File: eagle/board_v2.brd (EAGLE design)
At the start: 104.4 x 80.6 mm, 34 parts, among them J1 RJ11-4X, Q1 BD140, Q10 BD140, Q11 BD140, Q12 BD140, Q13 BD140, Q14 BD140, Q15 BD140, Q2 BD140, Q3 BD140, Q4 BD140, Q5 BD140, Q6 BD140, Q7 BD140, Q8 BD140, Q9 BD140, X1 RJ45-8X, X2 RJ45-8X, X3 RJ45-8X, X4 RJ45-8X, X5 RJ45-8X

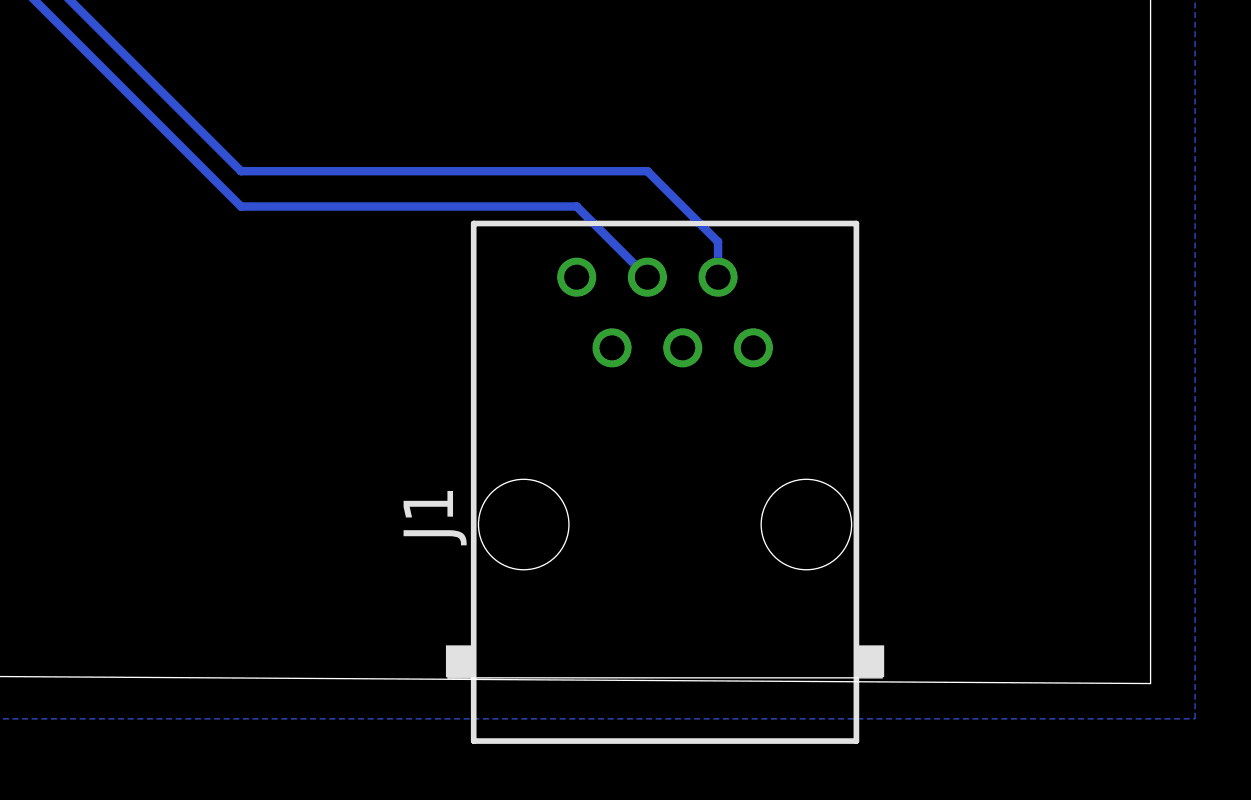
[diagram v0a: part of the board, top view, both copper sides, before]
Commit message: board chaining connectors
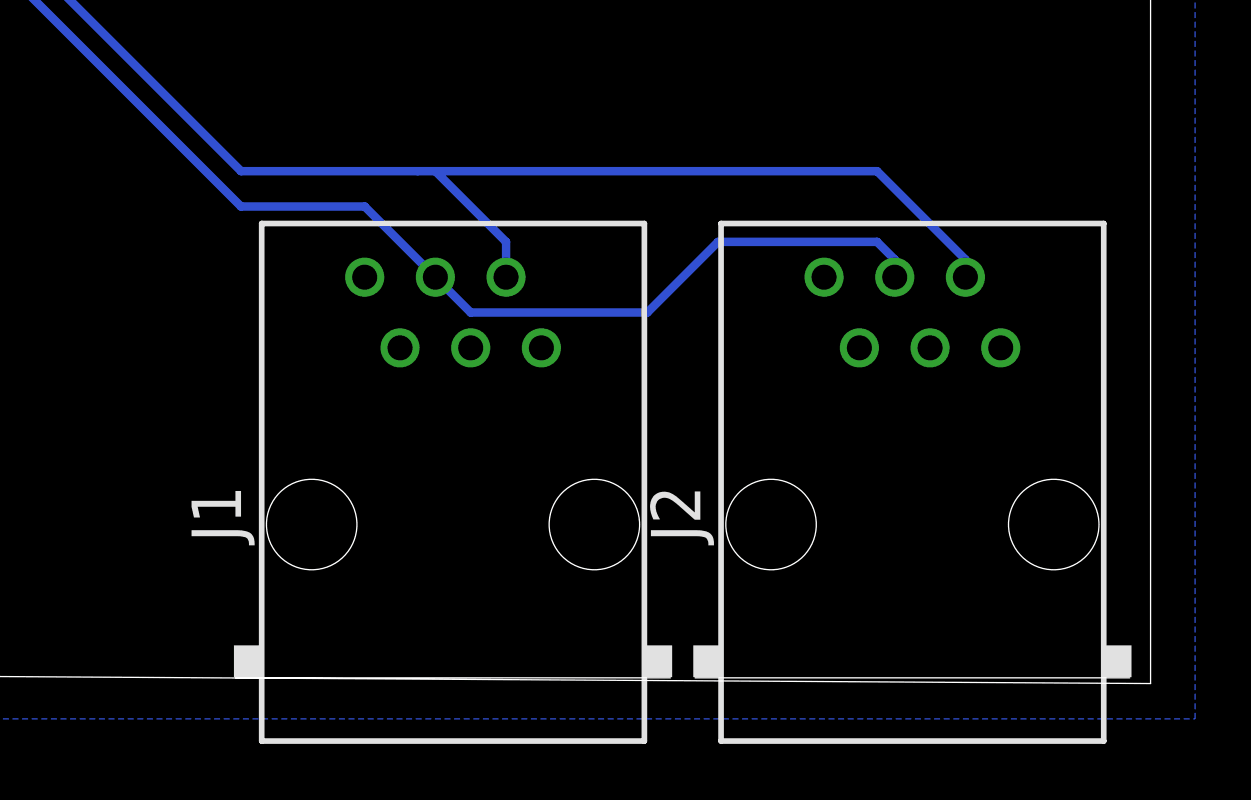
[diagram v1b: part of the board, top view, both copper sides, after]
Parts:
- added J2: RJ11-4X, con-tycoelectronics:RJ11-NO_SHIELD
- moved J1 7.62 mm to (79.4, 5.08)
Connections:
- net GND: now also J2.2, J2.4
- net N$37: now also J2.5
- net N$38: now also J2.3
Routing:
- net N$37: track 69.6 -> 83.0 mm
- net N$38: track 52.4 -> 63.8 mm
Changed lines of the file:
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@@
 <attribute name="OC_FARNELL" value="9471570" x="26.035" y="26.035" size="1.778" layer="27" rot="R90" display="off"/>
 </element>
-<element name="J1" library="con-tycoelectronics" package="RJ11-NO_SHIELD" value="RJ11-4X" x="86.995" y="5.08">
-<attribute name="OC_NEWARK" value="19R7022" x="86.995" y="5.08" size="2.54" layer="27" font="vector" display="off"/>
-<attribute name="MPN" value="6609214-3" x="86.995" y="5.08" size="2.54" layer="27" font="vector" display="off"/>
-<attribute name="MF" value="" x="86.995" y="5.08" size="2.54" layer="27" font="vector" display="off"/>
-<attribute name="OC_FARNELL" value="unknown" x="86.995" y="5.08" size="2.54" layer="27" font="vector" display="off"/>
+<element name="J1" library="con-tycoelectronics" package="RJ11-NO_SHIELD" value="RJ11-4X" x="79.375" y="5.08">
+<attribute name="OC_NEWARK" value="19R7022" x="79.375" y="5.08" size="2.54" layer="27" font="vector" display="off"/>
+<attribute name="MPN" value="6609214-3" x="79.375" y="5.08" size="2.54" layer="27" font="vector" display="off"/>
+<attribute name="MF" value="" x="79.375" y="5.08" size="2.54" layer="27" font="vector" display="off"/>
+<attribute name="OC_FARNELL" value="unknown" x="79.375" y="5.08" size="2.54" layer="27" font="vector" display="off"/>
+</element>
+<element name="J2" library="con-tycoelectronics" package="RJ11-NO_SHIELD" value="RJ11-4X" x="95.885" y="5.08">
+<attribute name="OC_NEWARK" value="19R7022" x="95.885" y="5.08" size="1.778" layer="27" display="off"/>
+<attribute name="MPN" value="6609214-3" x="95.885" y="5.08" size="1.778" layer="27" display="off"/>
+<attribute name="MF" value="" x="95.885" y="5.08" size="1.778" layer="27" display="off"/>
+<attribute name="OC_FARNELL" value="unknown" x="95.885" y="5.08" size="1.778" layer="27" display="off"/>
 </element>
 </elements>
@@
 <contactref element="J1" pad="4"/>
 <contactref element="J1" pad="2"/>
+<contactref element="J2" pad="4"/>
+<contactref element="J2" pad="2"/>
 </signal>
 <signal name="N$4">
@@
 <wire x1="45.237" y1="23.495" x2="45.085" y2="23.647" width="0.3048" layer="16"/>
 <contactref element="J1" pad="5"/>
-<wire x1="71.755" y1="17.78" x2="86.36" y2="17.78" width="0.3048" layer="16"/>
-<wire x1="86.36" y1="17.78" x2="88.9" y2="15.24" width="0.3048" layer="16"/>
-<wire x1="88.9" y1="15.24" x2="88.9" y2="13.97" width="0.3048" layer="16"/>
+<wire x1="71.755" y1="17.78" x2="78.105" y2="17.78" width="0.3048" layer="16"/>
+<wire x1="78.105" y1="17.78" x2="78.74" y2="17.78" width="0.3048" layer="16"/>
+<wire x1="78.74" y1="17.78" x2="81.28" y2="15.24" width="0.3048" layer="16"/>
+<wire x1="81.28" y1="15.24" x2="81.28" y2="13.97" width="0.3048" layer="16"/>
+<contactref element="J2" pad="5"/>
+<wire x1="97.79" y1="13.97" x2="97.79" y2="14.605" width="0.3048" layer="16"/>
+<wire x1="97.79" y1="14.605" x2="94.615" y2="17.78" width="0.3048" layer="16"/>
+<wire x1="94.615" y1="17.78" x2="78.74" y2="17.78" width="0.3048" layer="16"/>
 </signal>
 <signal name="N$38">
@@
 <wire x1="57.302" y1="30.963" x2="59.69" y2="28.575" width="0.3048" layer="16"/>
 <contactref element="J1" pad="3"/>
-<wire x1="71.755" y1="16.51" x2="83.82" y2="16.51" width="0.3048" layer="16"/>
-<wire x1="83.82" y1="16.51" x2="86.36" y2="13.97" width="0.3048" layer="16"/>
+<wire x1="71.755" y1="16.51" x2="76.2" y2="16.51" width="0.3048" layer="16"/>
+<wire x1="76.2" y1="16.51" x2="78.74" y2="13.97" width="0.3048" layer="16"/>
+<contactref element="J2" pad="3"/>
+<wire x1="95.25" y1="13.97" x2="95.25" y2="14.605" width="0.3048" layer="16"/>
+<wire x1="95.25" y1="14.605" x2="94.615" y2="15.24" width="0.3048" layer="16"/>
+<wire x1="94.615" y1="15.24" x2="88.9" y2="15.24" width="0.3048" layer="16"/>
+<wire x1="88.9" y1="15.24" x2="86.36" y2="12.7" width="0.3048" layer="16"/>
+<wire x1="86.36" y1="12.7" x2="80.01" y2="12.7" width="0.3048" layer="16"/>
+<wire x1="80.01" y1="12.7" x2="78.74" y2="13.97" width="0.3048" layer="16"/>
 </signal>
 <signal name="N$17">

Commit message: cinch -> svorkovnice
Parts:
- removed PWR: 736880-49, con-conrad:736880-49
- added GND, VCC: WIREPAD3,17/1,3, wirepad:3,17/1,3
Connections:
- net +5V: now also VCC.1; no longer PWR.1
- net GND: now also GND.1; no longer PWR.2
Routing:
- net +5V: track 285.2 -> 279.5 mm
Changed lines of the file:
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@@
 <setting verticaltext="up"/>
 </settings>
-<grid distance="0.635" unitdist="mm" unit="mm" style="lines" multiple="1" display="yes" altdistance="12.5" altunitdist="mil" altunit="mil"/>
+<grid distance="2.54" unitdist="mm" unit="mm" style="lines" multiple="1" display="yes" altdistance="12.5" altunitdist="mil" altunit="mil"/>
 <layers>
 <layer number="1" name="Top" color="4" fill="1" visible="yes" active="yes"/>
@@
 <element name="R3" library="resistor" package="R1206" value="10k" x="55.245" y="32.385" rot="MR90"/>
 <element name="U$1" library="tlc" package="TSSOP28" value="TLC59116" x="48.26" y="40.64" rot="MR90"/>
-<element name="PWR" library="con-conrad" package="736880-49" value="736880-49" x="13.335" y="7.62" rot="MR90"/>
 <element name="R4" library="resistor" package="R1206" value="10k" x="42.545" y="22.225" rot="MR270"/>
 <element name="C1" library="resistor" package="C1206" value="100n" x="52.07" y="32.385" rot="MR270"/>
@@
 <attribute name="OC_FARNELL" value="unknown" x="95.885" y="5.08" size="1.778" layer="27" display="off"/>
 </element>
+<element name="GND" library="wirepad" package="3,17/1,3" value="WIREPAD3,17/1,3" x="10.16" y="7.62"/>
+<element name="VCC" library="wirepad" package="3,17/1,3" value="WIREPAD3,17/1,3" x="15.24" y="7.62"/>
 </elements>
 <signals>
@@
 <contactref element="C1" pad="1"/>
 <contactref element="C2" pad="+"/>
-<contactref element="PWR" pad="1"/>
 <contactref element="R8" pad="1"/>
 <contactref element="R7" pad="1"/>
@@
 <wire x1="6.35" y1="18.415" x2="10.015" y2="18.415" width="1.016" layer="16"/>
 <wire x1="10.015" y1="18.415" x2="10.015" y2="17.29" width="1.016" layer="16"/>
-<wire x1="10.015" y1="17.29" x2="13.335" y2="13.97" width="1.016" layer="16"/>
-<wire x1="13.335" y1="13.97" x2="13.335" y2="5.715" width="1.016" layer="16"/>
-<wire x1="13.335" y1="5.715" x2="13.335" y2="3.7" width="1.016" layer="16"/>
+<wire x1="10.015" y1="17.29" x2="15.24" y2="12.065" width="1.016" layer="16"/>
 <wire x1="55.245" y1="33.807" x2="52.092" y2="33.807" width="0.3048" layer="16"/>
 <wire x1="52.092" y1="33.807" x2="52.07" y2="33.785" width="0.3048" layer="16"/>
 <wire x1="36.347" y1="31.75" x2="36.347" y2="20.32" width="0.3048" layer="16"/>
 <wire x1="36.347" y1="20.32" x2="36.347" y2="7.772" width="0.3048" layer="16"/>
-<wire x1="36.347" y1="7.772" x2="34.29" y2="5.715" width="0.3048" layer="16"/>
-<wire x1="34.29" y1="5.715" x2="13.335" y2="5.715" width="0.3048" layer="16"/>
 <wire x1="55.245" y1="33.807" x2="50.952" y2="33.807" width="0.3048" layer="16"/>
 <wire x1="50.952" y1="33.807" x2="49.53" y2="32.385" width="0.3048" layer="16"/>
@@
 <wire x1="45.085" y1="20.803" x2="45.085" y2="20.32" width="0.3048" layer="16"/>
 <wire x1="42.545" y1="20.803" x2="42.545" y2="20.32" width="0.3048" layer="16"/>
+<contactref element="VCC" pad="1"/>
+<wire x1="36.347" y1="7.772" x2="15.24" y2="7.772" width="0.3048" layer="16"/>
+<wire x1="15.24" y1="7.772" x2="15.24" y2="7.62" width="0.3048" layer="16"/>
+<wire x1="15.24" y1="12.065" x2="15.24" y2="7.62" width="1.016" layer="16"/>
 </signal>
 <signal name="N$1">
@@
 <vertex x="-1.905" y="81.28"/>
 </polygon>
-<contactref element="PWR" pad="2"/>
 <contactref element="C2" pad="-"/>
 <wire x1="51.1778" y1="39.015" x2="50.52" y2="39.015" width="0.3048" layer="16"/>
@@
 <contactref element="J2" pad="4"/>
 <contactref element="J2" pad="2"/>
+<contactref element="GND" pad="1"/>
 </signal>
 <signal name="N$4">

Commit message: moar changes
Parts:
- removed GND, VCC: WIREPAD3,17/1,3, wirepad:3,17/1,3
- added X6: RJ45-8X, con-tycoelectronics:RJ45-NO-SHIELD
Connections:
- net +5V: now also X6.1, X6.2, X6.3, X6.4; no longer VCC.1
- net GND: now also X6.5, X6.6, X6.7, X6.8; no longer GND.1
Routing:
- net +5V: track 279.5 -> 284.5 mm
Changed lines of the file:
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@@
 <setting verticaltext="up"/>
 </settings>
-<grid distance="2.54" unitdist="mm" unit="mm" style="lines" multiple="1" display="yes" altdistance="12.5" altunitdist="mil" altunit="mil"/>
+<grid distance="0.025" unitdist="inch" unit="inch" style="lines" multiple="1" display="yes" altdistance="0.0125" altunitdist="inch" altunit="inch"/>
 <layers>
 <layer number="1" name="Top" color="4" fill="1" visible="yes" active="yes"/>
@@
 <attribute name="OC_FARNELL" value="unknown" x="95.885" y="5.08" size="1.778" layer="27" display="off"/>
 </element>
-<element name="GND" library="wirepad" package="3,17/1,3" value="WIREPAD3,17/1,3" x="10.16" y="7.62"/>
-<element name="VCC" library="wirepad" package="3,17/1,3" value="WIREPAD3,17/1,3" x="15.24" y="7.62"/>
+<element name="X6" library="con-tycoelectronics" package="RJ45-NO-SHIELD" value="RJ45-8X" x="13.0175" y="5.3975">
+<attribute name="OC_NEWARK" value="16R6101" x="13.0175" y="5.3975" size="1.778" layer="27" display="off"/>
+<attribute name="MPN" value="RJ45-8X" x="13.0175" y="5.3975" size="1.778" layer="27" display="off"/>
+<attribute name="MF" value="" x="13.0175" y="5.3975" size="1.778" layer="27" display="off"/>
+<attribute name="OC_FARNELL" value="unknown" x="13.0175" y="5.3975" size="1.778" layer="27" display="off"/>
+</element>
 </elements>
 <signals>
@@
 <wire x1="4.445" y1="20.32" x2="6.35" y2="18.415" width="1.016" layer="16"/>
 <wire x1="6.35" y1="18.415" x2="10.015" y2="18.415" width="1.016" layer="16"/>
-<wire x1="10.015" y1="18.415" x2="10.015" y2="17.29" width="1.016" layer="16"/>
-<wire x1="10.015" y1="17.29" x2="15.24" y2="12.065" width="1.016" layer="16"/>
 <wire x1="55.245" y1="33.807" x2="52.092" y2="33.807" width="0.3048" layer="16"/>
 <wire x1="52.092" y1="33.807" x2="52.07" y2="33.785" width="0.3048" layer="16"/>
 <wire x1="36.347" y1="31.75" x2="36.347" y2="20.32" width="0.3048" layer="16"/>
-<wire x1="36.347" y1="20.32" x2="36.347" y2="7.772" width="0.3048" layer="16"/>
 <wire x1="55.245" y1="33.807" x2="50.952" y2="33.807" width="0.3048" layer="16"/>
 <wire x1="50.952" y1="33.807" x2="49.53" y2="32.385" width="0.3048" layer="16"/>
@@
 <wire x1="45.085" y1="20.803" x2="45.085" y2="20.32" width="0.3048" layer="16"/>
 <wire x1="42.545" y1="20.803" x2="42.545" y2="20.32" width="0.3048" layer="16"/>
-<contactref element="VCC" pad="1"/>
-<wire x1="36.347" y1="7.772" x2="15.24" y2="7.772" width="0.3048" layer="16"/>
-<wire x1="15.24" y1="7.772" x2="15.24" y2="7.62" width="0.3048" layer="16"/>
-<wire x1="15.24" y1="12.065" x2="15.24" y2="7.62" width="1.016" layer="16"/>
+<contactref element="X6" pad="1"/>
+<contactref element="X6" pad="2"/>
+<contactref element="X6" pad="3"/>
+<contactref element="X6" pad="4"/>
+<wire x1="11.1125" y1="11.7475" x2="11.1125" y2="8.89" width="0.3048" layer="16"/>
+<wire x1="11.1125" y1="8.89" x2="36.195" y2="8.89" width="0.3048" layer="16"/>
+<wire x1="36.195" y1="8.89" x2="36.347" y2="9.042" width="0.3048" layer="16"/>
+<wire x1="36.347" y1="9.042" x2="36.347" y2="20.32" width="0.3048" layer="16"/>
+<wire x1="9.8425" y1="14.2875" x2="10.015" y2="14.46" width="1.016" layer="16"/>
+<wire x1="10.015" y1="14.46" x2="10.015" y2="18.415" width="1.016" layer="16"/>
+<wire x1="9.8425" y1="14.2875" x2="12.3825" y2="14.2875" width="1.016" layer="16"/>
+<wire x1="12.3825" y1="14.2875" x2="11.1125" y2="13.0175" width="1.016" layer="16"/>
+<wire x1="11.1125" y1="13.0175" x2="11.1125" y2="11.7475" width="1.016" layer="16"/>
+<wire x1="11.1125" y1="11.7475" x2="8.5725" y2="11.7475" width="1.016" layer="16"/>
 </signal>
 <signal name="N$1">
@@
 <contactref element="J2" pad="4"/>
 <contactref element="J2" pad="2"/>
-<contactref element="GND" pad="1"/>
+<contactref element="X6" pad="6"/>
+<contactref element="X6" pad="8"/>
+<contactref element="X6" pad="7"/>
+<contactref element="X6" pad="5"/>
 </signal>
 <signal name="N$4">
